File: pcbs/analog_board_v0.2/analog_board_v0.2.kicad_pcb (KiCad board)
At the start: 2 copper layers, 80 x 50 mm, 95 parts, among them J1 CONN_02X03, J2 CONN_02X07, J3 CONN_01X04, P1 CONN_01X03, P2 CONN_01X03, P3 CONN_01X03, Q1 DMP2035U, Q2 TSM2314, Q3 DMP2035U, Q4 TSM2314, Q5 DMP2035U, Q6 TSM2314, Q7 DMP2035U, Q8 TSM2314, Q9 MMBT3904, U1 ADA4530-1, U2 ADA4522-2, U3 ICL7660S, U4 AD8616

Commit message: Analog board basically finished.
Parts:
- removed the REF** at (110.0, 120.0)
- added J4: CONN_01X01, Guard Connector:GuardConnector, F.Cu at (130.5, 128.0)
- added REF**: Stitching-Via-0.2-0.4, Vias:Stitchging-Via-0.2-0.4, F.Cu at (128.9, 129.9)
- added REF**: MountingHole_3.2mm_M3_DIN965, Mounting_Holes:MountingHole_3.2mm_M3_DIN965, F.Cu at (109.5, 110.0)
- added REF**: MountingHole_3.2mm_M3_DIN965, Mounting_Holes:MountingHole_3.2mm_M3_DIN965, F.Cu at (180.5, 110.2)
- moved U3 119.8 mm to (157.6, 126.2), turned to 270 degrees
- moved Q4 112.4 mm to (168.0, 118.3)
- moved Q3 111.7 mm to (168.0, 113.8)
- moved Q5 111.6 mm to (171.5, 121.2)
- moved C19 109.0 mm to (163.7, 125.4), turned to 270 degrees
- moved Q6 108.4 mm to (171.5, 125.6)
- moved P2 103.5 mm to (149.9, 91.2)
- moved Q7 101.2 mm to (163.5, 113.8)
- moved Q2 100.4 mm to (176.0, 125.6)
- moved TP6 97.9 mm to (163.1, 129.8)
- moved TP4 97.1 mm to (176.4, 114.9)
- moved Q8 96.7 mm to (163.5, 118.3)
- moved TP7 93.7 mm to (172.0, 114.9)
- moved C17 92.5 mm to (151.5, 126.9), turned to 270 degrees
- moved C18 88.4 mm to (160.7, 130.7), turned to 270 degrees
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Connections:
- J1 pad 1: +5V -> GND
- J1 pad 2: GND -> +5V
- J1 pad 3: /interface/ADC1 -> /interface/ADC3
- J1 pad 4: /interface/ADC3 -> /interface/ADC1
- J1 pad 5: /interface/ADC2 -> /interface/ADC4
- J1 pad 6: /interface/ADC4 -> /interface/ADC2
- J2 pad 1: +3V3 -> /interface/DAC1
- J2 pad 10: /interface/GPIO4 -> /interface/GPIO2
- J2 pad 11: (no net) -> GND
- J2 pad 12: (no net) -> /interface/GPIO1
- J2 pad 13: /interface/DAC1 -> +3V3
- J2 pad 14: /interface/DAC2 -> (no net)
- J2 pad 2: (no net) -> /interface/DAC2
- J2 pad 3: GND -> (no net)
- J2 pad 4: /interface/GPIO1 -> (no net)
- J2 pad 5: /interface/I2C_SCL -> (no net)
- J2 pad 6: /interface/GPIO2 -> /interface/GPIO4
- J2 pad 9: (no net) -> /interface/I2C_SCL
- P1 pad 2: (no net) -> Net-(P1-Pad2)
- P1 pad 3: Net-(P1-Pad3) -> (no net)
- U3 pad 1: Net-(P1-Pad3) -> Net-(P1-Pad2)
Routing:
- net +5V: track 0.00 -> 195.0 mm, vias 0 -> 7
- net +3V3: track 12.9 -> 95.6 mm, vias 0 -> 2
- net /highCurrentPart/-3.3V: track 11.7 -> 91.4 mm, vias 1 -> 2
- net /interface/GPIO1: track 0.00 -> 75.8 mm
- net /interface/GPIO2: track 0.00 -> 73.7 mm
- net Net-(R4-Pad2): track 6.26 -> 75.6 mm
- net /interface/GPIO3: track 0.00 -> 53.9 mm
- net /interface/ADC4: track 0.00 -> 53.8 mm, vias 0 -> 1
- net Net-(C7-Pad1): track 20.6 -> 71.9 mm
- net /interface/GPIO4: track 0.00 -> 51.1 mm
- net Signal: track 0.00 -> 44.8 mm
- net /interface/DAC1: track 0.00 -> 32.8 mm
- net COIL_4: track 0.00 -> 20.1 mm
- net COIL_3: track 0.00 -> 19.4 mm
- net Net-(C23-Pad1): track 0.00 -> 14.8 mm
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- added copper zone on B.Cu, net GND
- added copper zone on F.Cu, net GND
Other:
- outline, holes or cut-outs redrawn

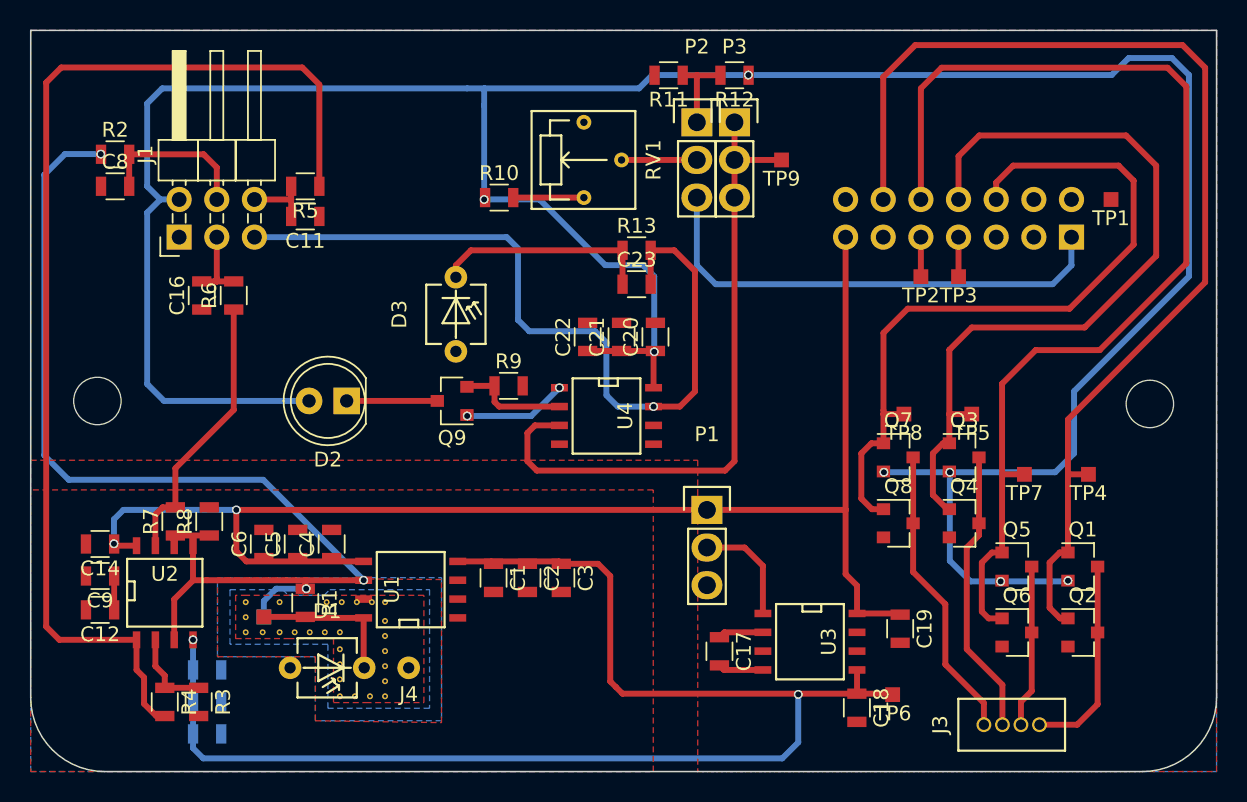
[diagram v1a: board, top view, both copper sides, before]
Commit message: Small changes on the backplane standing out.
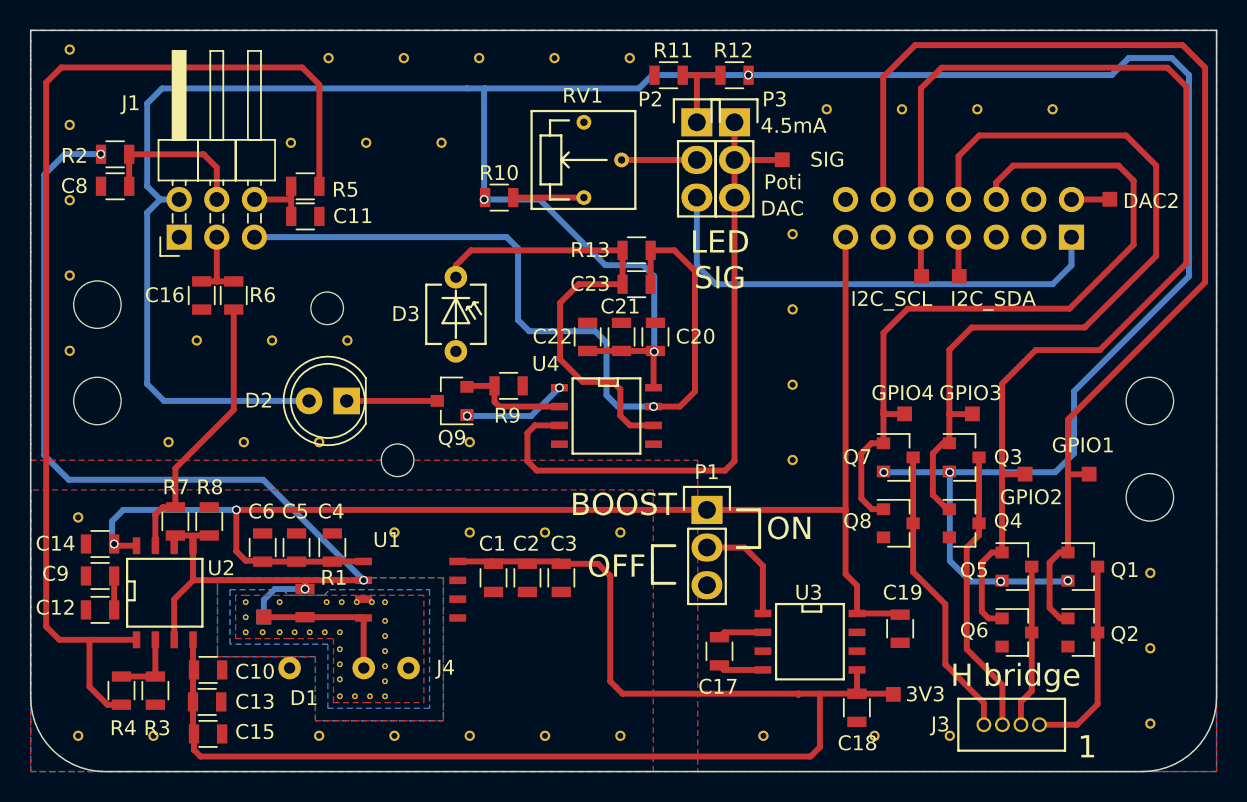
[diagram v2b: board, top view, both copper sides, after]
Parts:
- removed TP1, TP2, TP3, TP4, TP5, TP6, TP7, TP8, TP9: TEST, Tespoints:TP_SMD_quadr_1mm
- added 3V3: TEST, Tespoints:TP_SMD_quadr_1mm, F.Cu at (163.2, 129.8)
- added DAC2: DAC2, Tespoints:TP_SMD_quadr_1mm, F.Cu at (177.8, 96.4)
- added GPIO1: TEST, Tespoints:TP_SMD_quadr_1mm, F.Cu at (176.4, 114.9)
- added GPIO2: TEST, Tespoints:TP_SMD_quadr_1mm, F.Cu at (172.1, 114.9)
- added GPIO3: TEST, Tespoints:TP_SMD_quadr_1mm, F.Cu at (168.5, 110.9)
- added GPIO4: TEST, Tespoints:TP_SMD_quadr_1mm, F.Cu at (164.0, 110.9)
- added I2C_SCL: TEST, Tespoints:TP_SMD_quadr_1mm, F.Cu at (165.1, 101.6)
- added I2C_SDA: TEST, Tespoints:TP_SMD_quadr_1mm, F.Cu at (167.6, 101.6)
- added REF**: Stitching-Via-0.4-0.7, Vias:Stitchging-Via-0.4-0.7, F.Cu at (134.6, 112.8)
- added REF**: Stitching-Via-0.4-0.7, Vias:Stitchging-Via-0.4-0.7, F.Cu at (173.9, 90.3)
- added REF**: Stitching-Via-0.4-0.7, Vias:Stitchging-Via-0.4-0.7, F.Cu at (163.8, 90.3)
- added REF**: Stitching-Via-0.4-0.7, Vias:Stitchging-Via-0.4-0.7, F.Cu at (168.9, 90.3)
- added REF**: Stitching-Via-0.4-0.7, Vias:Stitchging-Via-0.4-0.7, F.Cu at (158.7, 90.3)
- added REF**: Stitching-Via-0.4-0.7, Vias:Stitchging-Via-0.4-0.7, F.Cu at (108.2, 117.9)
- added REF**: Stitching-Via-0.4-0.7, Vias:Stitchging-Via-0.4-0.7, F.Cu at (108.2, 132.6)
- added REF**: Stitching-Via-0.4-0.7, Vias:Stitchging-Via-0.4-0.7, F.Cu at (113.3, 132.6)
- added REF**: Stitching-Via-0.4-0.7, Vias:Stitchging-Via-0.4-0.7, F.Cu at (154.4, 132.6)
- added REF**: Stitching-Via-0.4-0.7, Vias:Stitchging-Via-0.4-0.7, F.Cu at (161.9, 132.6)
- added REF**: Stitching-Via-0.4-0.7, Vias:Stitchging-Via-0.4-0.7, F.Cu at (167.0, 132.6)
- added REF**: Stitching-Via-0.4-0.7, Vias:Stitchging-Via-0.4-0.7, F.Cu at (124.5, 112.8)
- added REF**: Stitching-Via-0.4-0.7, Vias:Stitchging-Via-0.4-0.7, F.Cu at (126.4, 105.9)
- added REF**: Stitching-Via-0.4-0.7, Vias:Stitchging-Via-0.4-0.7, F.Cu at (116.2, 105.9)
- added REF**: Stitching-Via-0.4-0.7, Vias:Stitchging-Via-0.4-0.7, F.Cu at (121.3, 105.9)
- added REF**: Stitching-Via-0.4-0.7, Vias:Stitchging-Via-0.4-0.7, F.Cu at (132.7, 92.6)
- added REF**: Stitching-Via-0.4-0.7, Vias:Stitchging-Via-0.4-0.7, F.Cu at (122.6, 92.6)
- added REF**: Stitching-Via-0.4-0.7, Vias:Stitchging-Via-0.4-0.7, F.Cu at (127.6, 92.6)
- added REF**: Stitching-Via-0.4-0.7, Vias:Stitchging-Via-0.4-0.7, F.Cu at (145.4, 86.9)
- added REF**: Stitching-Via-0.4-0.7, Vias:Stitchging-Via-0.4-0.7, F.Cu at (135.3, 86.9)
- added REF**: Stitching-Via-0.4-0.7, Vias:Stitchging-Via-0.4-0.7, F.Cu at (140.3, 86.9)
- added REF**: Stitching-Via-0.4-0.7, Vias:Stitchging-Via-0.4-0.7, F.Cu at (130.2, 86.9)
- added REF**: Stitching-Via-0.4-0.7, Vias:Stitchging-Via-0.4-0.7, F.Cu at (119.4, 112.8)
- added REF**: Stitching-Via-0.4-0.7, Vias:Stitchging-Via-0.4-0.7, F.Cu at (125.1, 86.9)
- added REF**: Stitching-Via-0.4-0.7, Vias:Stitchging-Via-0.4-0.7, F.Cu at (180.5, 121.6)
- added REF**: Stitching-Via-0.4-0.7, Vias:Stitchging-Via-0.4-0.7, F.Cu at (180.5, 131.8)
- added REF**: Stitching-Via-0.4-0.7, Vias:Stitchging-Via-0.4-0.7, F.Cu at (180.5, 126.7)
- added REF**: Stitching-Via-0.4-0.7, Vias:Stitchging-Via-0.4-0.7, F.Cu at (156.4, 98.7)
- added REF**: Stitching-Via-0.4-0.7, Vias:Stitchging-Via-0.4-0.7, F.Cu at (156.4, 108.9)
- added REF**: Stitching-Via-0.4-0.7, Vias:Stitchging-Via-0.4-0.7, F.Cu at (156.4, 103.8)
- added REF**: Stitching-Via-0.4-0.7, Vias:Stitchging-Via-0.4-0.7, F.Cu at (156.4, 114.0)
- added REF**: Stitching-Via-0.4-0.7, Vias:Stitchging-Via-0.4-0.7, F.Cu at (129.5, 118.9)
- added REF**: Stitching-Via-0.4-0.7, Vias:Stitchging-Via-0.4-0.7, F.Cu at (144.8, 118.9)
- added REF**: Stitching-Via-0.4-0.7, Vias:Stitchging-Via-0.4-0.7, F.Cu at (114.3, 112.8)
- added REF**: Stitching-Via-0.4-0.7, Vias:Stitchging-Via-0.4-0.7, F.Cu at (134.6, 118.9)
- added REF**: Stitching-Via-0.4-0.7, Vias:Stitchging-Via-0.4-0.7, F.Cu at (139.7, 118.9)
- added REF**: Stitching-Via-0.4-0.7, Vias:Stitchging-Via-0.4-0.7, F.Cu at (124.5, 132.6)
- added REF**: Stitching-Via-0.4-0.7, Vias:Stitchging-Via-0.4-0.7, F.Cu at (129.5, 132.6)
- added REF**: Stitching-Via-0.4-0.7, Vias:Stitchging-Via-0.4-0.7, F.Cu at (139.7, 132.6)
- added REF**: Stitching-Via-0.4-0.7, Vias:Stitchging-Via-0.4-0.7, F.Cu at (134.6, 132.6)
- added REF**: MountingHole_3.2mm_M3_DIN965, Mounting_Holes:MountingHole_3.2mm_M3_DIN965, F.Cu at (109.5, 103.5)
- added REF**: MountingHole_3.2mm_M3_DIN965, Mounting_Holes:MountingHole_3.2mm_M3_DIN965, F.Cu at (180.5, 116.5)
- added REF**: Stitching-Via-0.4-0.7, Vias:Stitchging-Via-0.4-0.7, F.Cu at (107.6, 86.3)
- added REF**: Stitching-Via-0.4-0.7, Vias:Stitchging-Via-0.4-0.7, F.Cu at (107.6, 96.5)
- added REF**: Stitching-Via-0.4-0.7, Vias:Stitchging-Via-0.4-0.7, F.Cu at (107.6, 91.4)
- added REF**: MountingHole_2.2mm_M2, Mounting_Holes:MountingHole_2.2mm_M2, F.Cu at (129.8, 114.0)
- added REF**: MountingHole_2.2mm_M2, Mounting_Holes:MountingHole_2.2mm_M2, F.Cu at (125.0, 103.8)
- added REF**: Stitching-Via-0.4-0.7, Vias:Stitchging-Via-0.4-0.7, F.Cu at (144.8, 132.6)
- added REF**: Stitching-Via-0.4-0.7, Vias:Stitchging-Via-0.4-0.7, F.Cu at (107.6, 101.5)
- added REF**: Stitching-Via-0.4-0.7, Vias:Stitchging-Via-0.4-0.7, F.Cu at (107.6, 106.6)
- added SIG: TEST, Tespoints:TP_SMD_quadr_1mm, F.Cu at (155.7, 93.7)
- C10, C13, C15: moved to F.Cu
- D1: footprint Photodiodes:BPW34FA -> Photodiodes:BPW34FA_w_Silks
- R1: footprint Resistors_SMD:R_0805 -> WithoutSilkscreen:R_0805_W_Silks
- U1: footprint SMD_Packages:SOIC-8-N -> WithoutSilkscreen:SOIC-8-N-W-Silks
- moved R4 3.02 mm to (111.1, 129.5)
- moved R3 3.02 mm to (113.4, 129.5)
- moved C5 0.25 mm to (122.9, 119.9)
- moved C6 0.25 mm to (120.7, 119.9)
- moved C4 0.24 mm to (125.3, 119.9)
- moved REF** 0.20 mm to (180.5, 110.0)
- moved C10 0.06 mm to (117.0, 128.1)
- moved C15 0.06 mm to (117.0, 132.5)
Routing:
- net Net-(C23-Pad1): track 14.8 -> 32.5 mm
- net /interface/DAC2: track 0.00 -> 2.59 mm
- net /highCurrentPart/-3.3V: track 91.4 -> 93.0 mm, vias 2 -> 0
- net Net-(R3-Pad1): track 5.79 -> 4.77 mm
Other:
- board text added: "1"
- board text added: "4.5mA"
- board text added: "BOOST"
- board text added: "DAC"
- board text added: "H bridge"
- board text added: "LED SIG"
- board text added: "OFF"
- board text added: "ON"
- board text added: "Poti"

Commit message: Backplane definitely finished. Somethings wrong with TIA. Has to be checked tomorrow.
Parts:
- moved U1 21.1 mm to (142.8, 140.0), turned to 270 degrees
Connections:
- C20 pad 1: +5V -> +3V3
- C21 pad 1: +5V -> +3V3
- C22 pad 1: +5V -> +3V3
- U4 pad 8: +5V -> +3V3
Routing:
- net +5V: track 195.0 -> 169.1 mm, vias 7 -> 6
- net +3V3: track 95.9 -> 116.0 mm, vias 2 -> 4
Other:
- board text added: "Distance 1st pin TSW-103-08-G-D-RA to plastic 1.52 mm + Thickness Plastic 2.54 mm + Deepness female connector BCS-103-F-D-TE 7.37 mm -------------------------------------- 11.43 mm -> PCB sits directly on backplane."
- board text added: "FREQUENCY BOOST"
- board text removed: "BOOST"
